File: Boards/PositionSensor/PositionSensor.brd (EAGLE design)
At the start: 12.7 x 22.5 mm, 4 parts

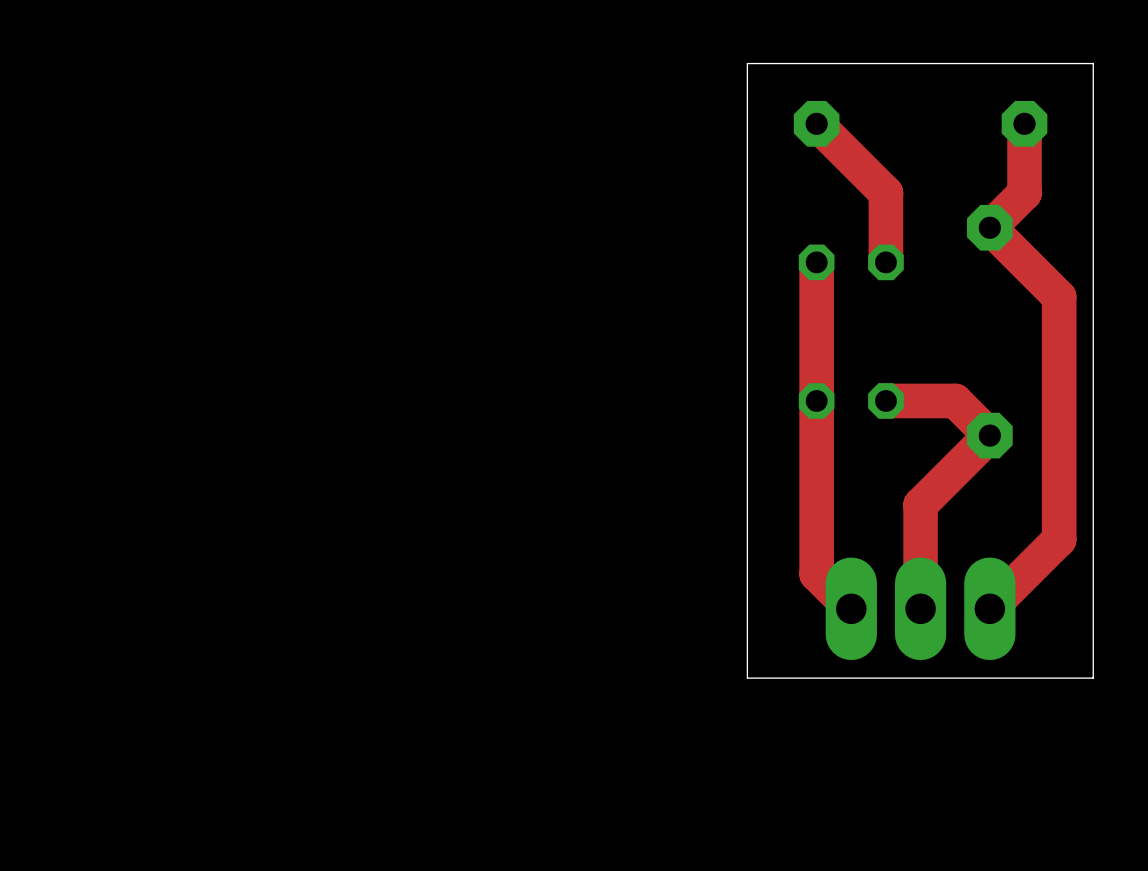
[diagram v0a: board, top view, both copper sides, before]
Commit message: updated position sensor
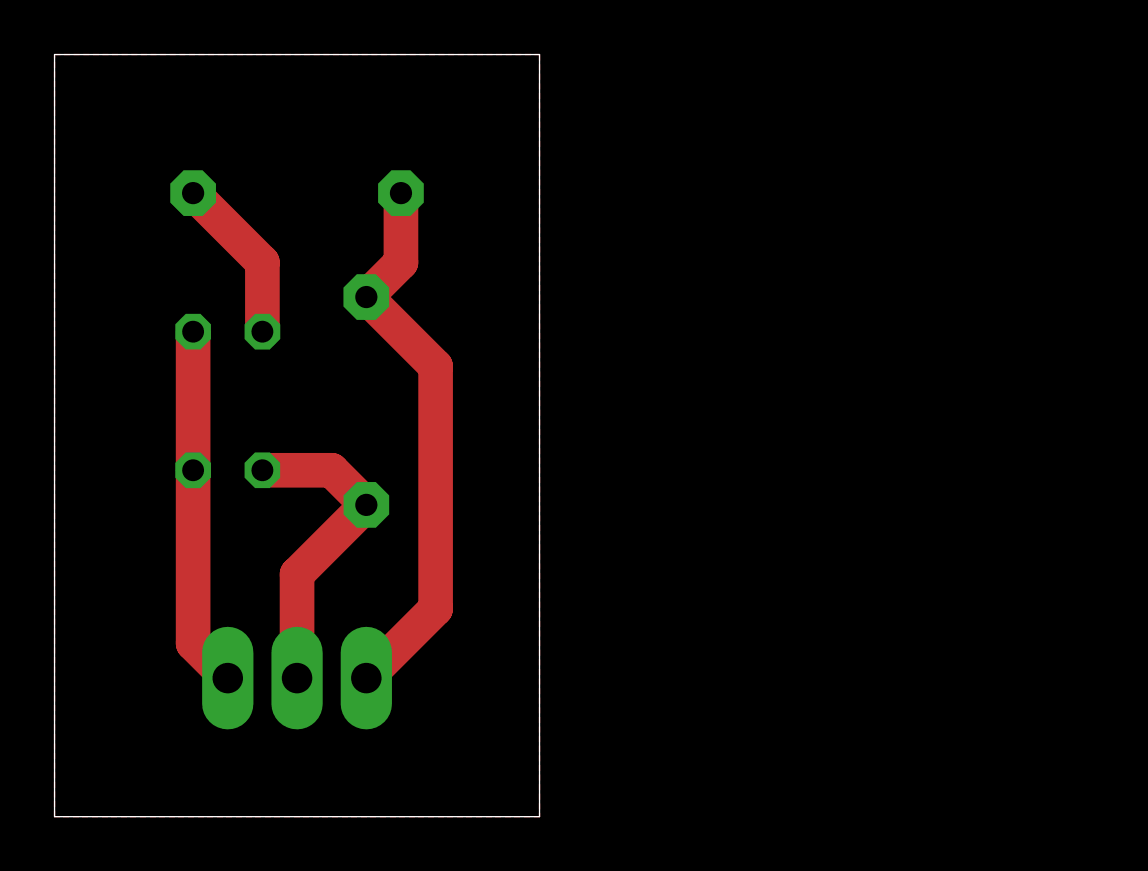
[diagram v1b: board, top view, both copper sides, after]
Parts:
- moved J1 23.0 mm to (11.4, 5.08)
- moved R1 23.0 mm to (11.4, 15.2)
- moved R2 23.0 mm to (8.89, 22.9)
- moved TC1 23.0 mm to (6.35, 15.2)
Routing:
- added copper zone on layer 1, net N$2
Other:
- board size 12.7 x 22.5 mm -> 17.8 x 27.9 mm
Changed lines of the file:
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@@
 <setting verticaltext="up"/>
 </settings>
-<grid distance="0.05" unitdist="inch" unit="mm" style="lines" multiple="1" display="no" altdistance="0.025" altunitdist="inch" altunit="inch"/>
+<grid distance="0.05" unitdist="inch" unit="mm" style="lines" multiple="1" display="yes" altdistance="0.025" altunitdist="inch" altunit="inch"/>
 <layers>
 <layer number="1" name="Top" color="4" fill="1" visible="yes" active="yes"/>
@@
 <board>
 <plain>
-<wire x1="25.4" y1="5.08" x2="38.08" y2="5.08" width="0" layer="20"/>
-<wire x1="38.08" y1="5.08" x2="38.08" y2="27.61" width="0" layer="20"/>
-<wire x1="38.08" y1="27.61" x2="25.4" y2="27.61" width="0" layer="20"/>
-<wire x1="25.4" y1="27.61" x2="25.4" y2="5.08" width="0" layer="20"/>
+<wire x1="0" y1="0" x2="17.78" y2="0" width="0" layer="20"/>
+<wire x1="17.78" y1="0" x2="17.78" y2="27.94" width="0" layer="20"/>
+<wire x1="17.78" y1="27.94" x2="0" y2="27.94" width="0" layer="20"/>
+<wire x1="0" y1="27.94" x2="0" y2="0" width="0" layer="20"/>
 </plain>
 <attributes>
@@
 </autorouter>
 <elements>
-<element name="R1" library="adafruit" package="0204/7" value="22K" x="34.29" y="17.78" rot="MR90"/>
-<element name="R2" library="adafruit" package="0204/7" value="47R" x="31.75" y="25.4" rot="MR0"/>
-<element name="J1" library="SparkFun-Connectors" package="1X03_LONGPADS" value="" x="34.29" y="7.62" rot="MR0"/>
-<element name="TC1" library="Library" package="TCRT5000" value="TCRT5000" x="29.21" y="17.78" rot="MR0"/>
+<element name="R1" library="adafruit" package="0204/7" value="22K" x="11.43" y="15.24" rot="MR90"/>
+<element name="R2" library="adafruit" package="0204/7" value="47R" x="8.89" y="22.86" rot="MR0"/>
+<element name="J1" library="SparkFun-Connectors" package="1X03_LONGPADS" value="" x="11.43" y="5.08" rot="MR0"/>
+<element name="TC1" library="Library" package="TCRT5000" value="TCRT5000" x="6.35" y="15.24" rot="MR0"/>
 </elements>
 <signals>
@@
 <contactref element="R2" pad="2"/>
 <contactref element="TC1" pad="A"/>
-<wire x1="30.48" y1="20.32" x2="30.48" y2="22.86" width="1.27" layer="1"/>
-<wire x1="30.48" y1="22.86" x2="27.94" y2="25.4" width="1.27" layer="1"/>
+<wire x1="7.62" y1="17.78" x2="7.62" y2="20.32" width="1.27" layer="1"/>
+<wire x1="7.62" y1="20.32" x2="5.08" y2="22.86" width="1.27" layer="1"/>
 </signal>
 <signal name="VCC">
@@
 <contactref element="R2" pad="1"/>
 <contactref element="J1" pad="1"/>
-<wire x1="35.56" y1="25.4" x2="35.56" y2="22.86" width="1.27" layer="1"/>
-<wire x1="35.56" y1="22.86" x2="34.29" y2="21.59" width="1.27" layer="1"/>
-<wire x1="34.29" y1="21.59" x2="36.83" y2="19.05" width="1.27" layer="1"/>
-<wire x1="36.83" y1="19.05" x2="36.83" y2="10.16" width="1.27" layer="1"/>
-<wire x1="36.83" y1="10.16" x2="34.29" y2="7.62" width="1.27" layer="1"/>
+<wire x1="12.7" y1="22.86" x2="12.7" y2="20.32" width="1.27" layer="1"/>
+<wire x1="12.7" y1="20.32" x2="11.43" y2="19.05" width="1.27" layer="1"/>
+<wire x1="11.43" y1="19.05" x2="13.97" y2="16.51" width="1.27" layer="1"/>
+<wire x1="13.97" y1="16.51" x2="13.97" y2="7.62" width="1.27" layer="1"/>
+<wire x1="13.97" y1="7.62" x2="11.43" y2="5.08" width="1.27" layer="1"/>
 </signal>
 <signal name="GND">
@@
 <contactref element="TC1" pad="E"/>
 <contactref element="J1" pad="3"/>
-<wire x1="27.94" y1="20.32" x2="27.94" y2="15.24" width="1.27" layer="1"/>
-<wire x1="27.94" y1="15.24" x2="27.94" y2="8.89" width="1.27" layer="1"/>
-<wire x1="27.94" y1="8.89" x2="29.21" y2="7.62" width="1.27" layer="1"/>
+<wire x1="5.08" y1="17.78" x2="5.08" y2="12.7" width="1.27" layer="1"/>
+<wire x1="5.08" y1="12.7" x2="5.08" y2="6.35" width="1.27" layer="1"/>
+<wire x1="5.08" y1="6.35" x2="6.35" y2="5.08" width="1.27" layer="1"/>
 </signal>
 <signal name="SIG">
@@
 <contactref element="TC1" pad="C"/>
 <contactref element="R1" pad="1"/>
-<wire x1="30.48" y1="15.24" x2="33.02" y2="15.24" width="1.27" layer="1"/>
-<wire x1="33.02" y1="15.24" x2="34.29" y2="13.97" width="1.27" layer="1"/>
-<wire x1="31.75" y1="7.62" x2="31.75" y2="11.43" width="1.27" layer="1"/>
-<wire x1="31.75" y1="11.43" x2="34.29" y2="13.97" width="1.27" layer="1"/>
+<wire x1="7.62" y1="12.7" x2="10.16" y2="12.7" width="1.27" layer="1"/>
+<wire x1="10.16" y1="12.7" x2="11.43" y2="11.43" width="1.27" layer="1"/>
+<wire x1="8.89" y1="5.08" x2="8.89" y2="8.89" width="1.27" layer="1"/>
+<wire x1="8.89" y1="8.89" x2="11.43" y2="11.43" width="1.27" layer="1"/>
+</signal>
+<signal name="N$2">
+<polygon width="0.18" layer="1" isolate="0.525" orphans="yes" rank="6">
+<vertex x="0" y="27.94"/>
+<vertex x="17.78" y="27.94"/>
+<vertex x="17.78" y="0"/>
+<vertex x="0" y="0"/>
+</polygon>
 </signal>
 </signals>

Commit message: finished for mass production
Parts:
- added U$1: (no value), SparkFun-Hardware:STAND-OFF
- moved R2 16.7 mm to (11.4, 6.35), flipped to the top, turned to 90 degrees
- moved J1 15.9 mm to (27.3, 3.81), flipped to the top, turned to 90 degrees
- moved TC1 14.5 mm to (19.1, 8.26), flipped to the top, turned to 90 degrees
- moved R1 14.3 mm to (19.1, 3.17), flipped to the top, turned to 180 degrees
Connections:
- net VCC renamed 3V3
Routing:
- net 3V3: track 20.4 -> 0.00 mm
- net GND: track 13.2 -> 0.00 mm
- net SIG: track 11.7 -> 11.1 mm
- added copper zone on layer 1, net 3V3
- added copper zone on layer 16, net GND
- removed copper zone on layer 1, net N$2
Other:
- board size 17.8 x 27.9 mm -> 34.3 x 12.7 mm
- board text added: "GND SIG 3V3"
- board text added: "IAD Lab"
- board text added: "TCRT5000"
